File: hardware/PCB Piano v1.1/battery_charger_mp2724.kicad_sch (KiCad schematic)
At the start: 25 parts, among them J2 JST PH 4-PIN, J5 PinHeader 1x02 SMT, SW5 JST-PH 1x03 SMT, U15 MP2724GRH-0000-P

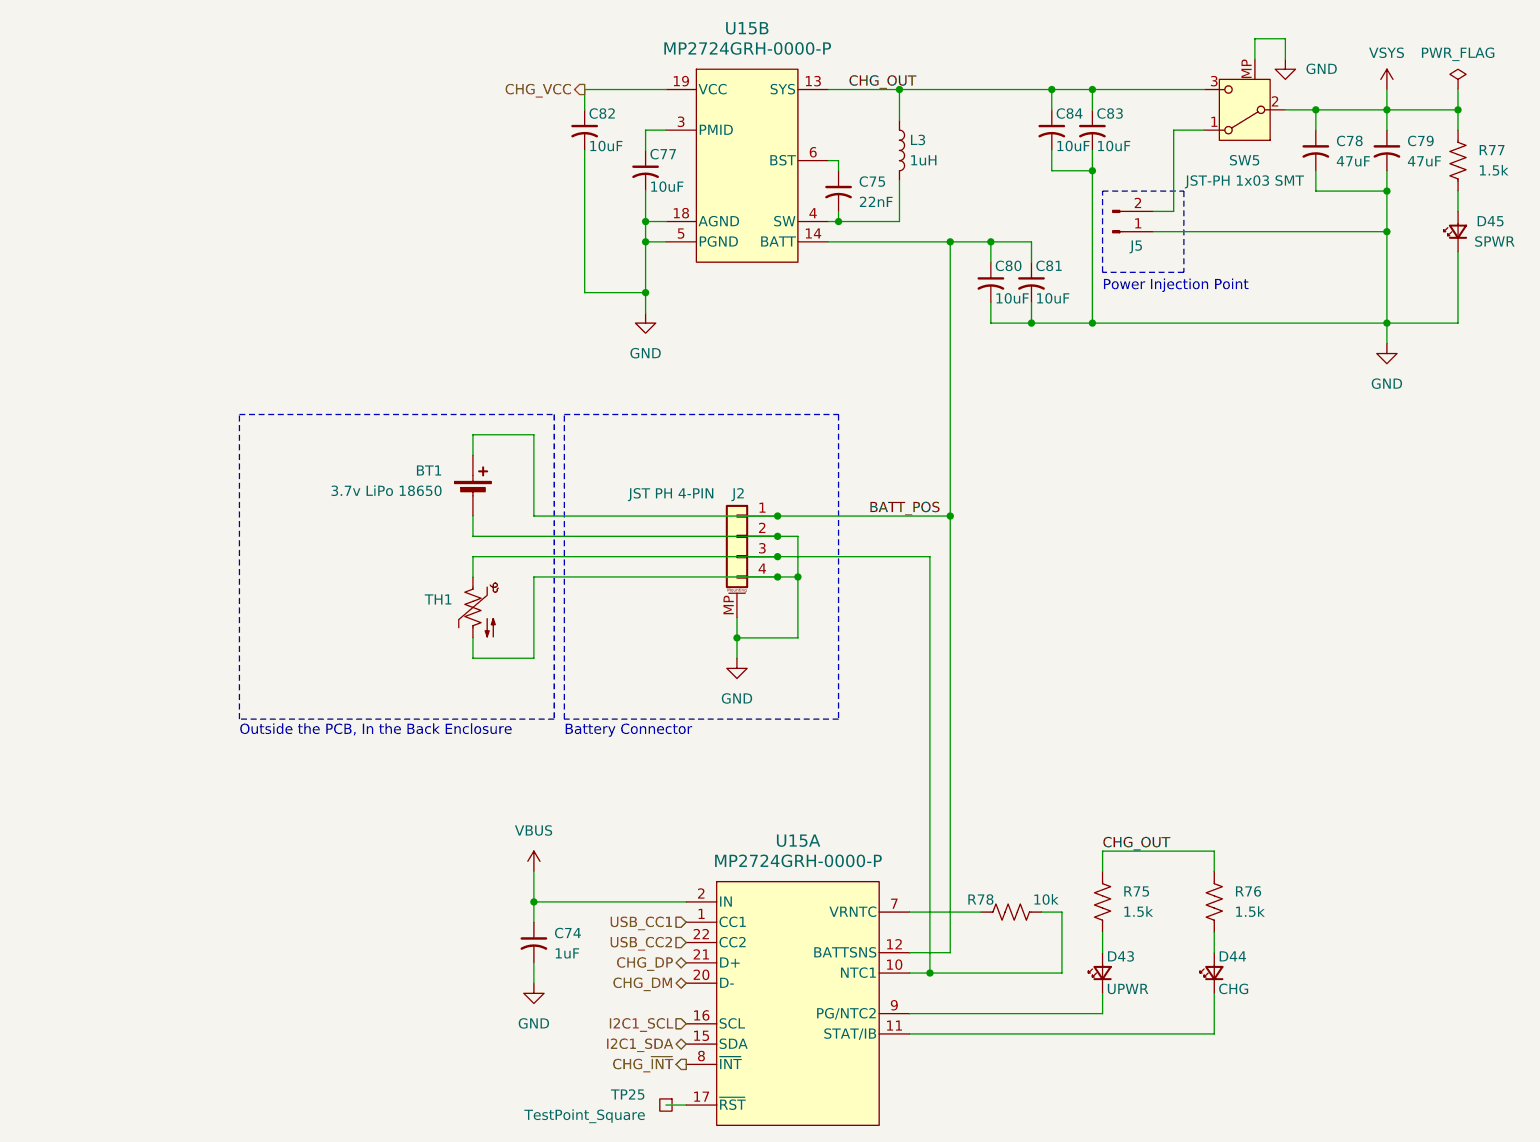
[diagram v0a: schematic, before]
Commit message: PCB Finalized and Ordered. Firmware near completion.
PCB Finalized and Ordered. Final revisions included fixing bugs on some peripheral chips. Also added an RTC circuit after realizing the SD card could benefit from adding file timestamps.

Firmware near completion. Still need to finalize some SD card operations. Synth audio core is finished and all the board peripheral chip drivers were completed.
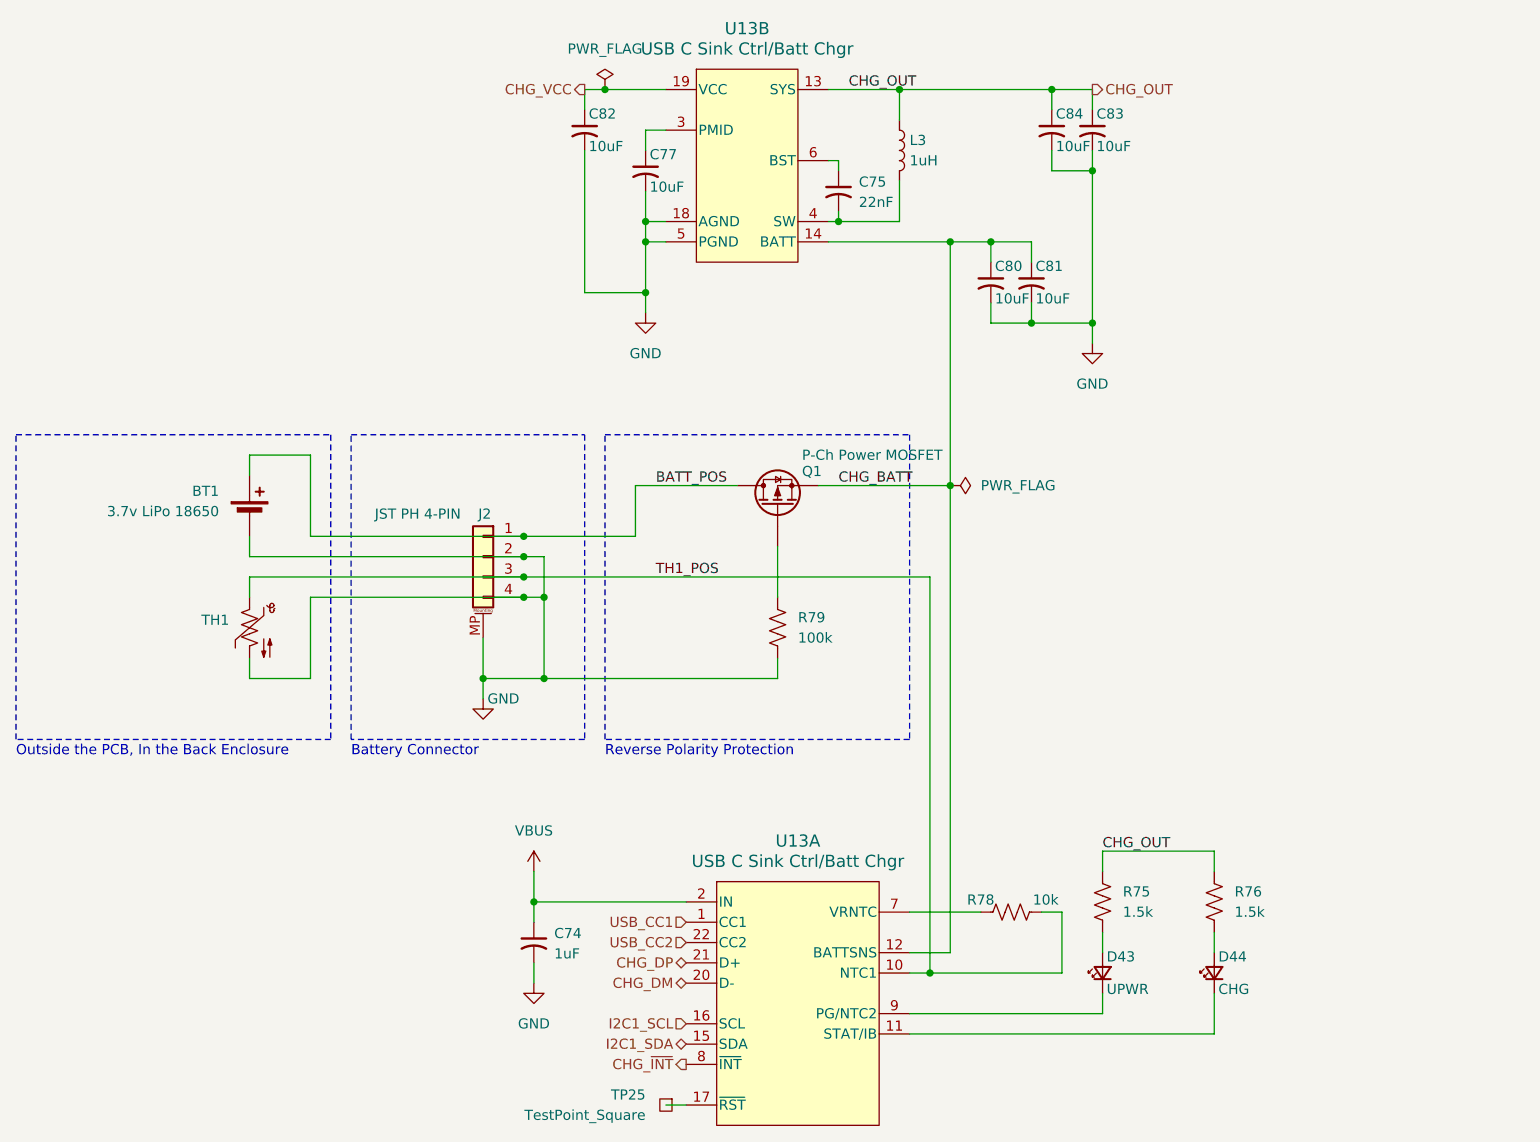
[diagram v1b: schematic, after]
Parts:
- removed C78, C79: 47uF, Capacitor_Tantalum_SMD:CP_EIA-3528-15_AVX-H, symbol Device:C_Small_US
- removed D45: LTST-C191TBKT, PCBPiano_Footprints:LED_0603_1608Metric, symbol Device:LED_Small
- removed J5: PinHeader 1x02 SMT, Connector_PinHeader_2.54mm:PinHeader_1x02_P2.54mm_Vertical_SMD_Pin1Left, symbol Connector:Conn_01x02_Pin
- removed R77: 1.5k, Resistor_SMD:R_0603_1608Metric, symbol Device:R_US
- removed SW5: JST-PH 1x03 SMT, Connector_JST:JST_PH_B3B-PH-SM4-TB_1x03-1MP_P2.00mm_Vertical, symbol PCB Piano Symbols:SW_SPDT_MP
- added Q1: P-Ch Power MOSFET, PCBPiano_Footprints:PPAK_3x3, symbol Device:Q_PMOS
- added R79: 100k, Resistor_SMD:R_0603_1608Metric, symbol Device:R_US
- C74: DigiKey_Part_Number (none) -> 1276-1184-1-ND; Manufacturer Part Number (none) -> CL10B105KA8NNNC; Volt Rating (none) -> 25V
- C75: footprint Capacitor_SMD:C_0603_1608Metric -> Capacitor_SMD:C_0805_2012Metric; DigiKey_Part_Number (none) -> 490-10516-1-ND; Manufacturer Part Number (none) -> GRM21B5C1H223JA01L; Volt Rating 16V -> 10V
- C77: DigiKey_Part_Number (none) -> 490-GRM21BZ71E106KE15LCT-ND; Manufacturer Part Number (none) -> GRM21BZ71E106KE15L
- C80, C81, C83, C84: DigiKey_Part_Number (none) -> 490-10516-1-ND; Manufacturer Part Number (none) -> GRM21BR71A106KA73L GRM21BR71A106KA73L GRM21BR71A106KA73L GR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; Volt Rating 16V -> 10V
- C82: DigiKey_Part_Number (none) -> 490-10516-1-ND; Manufacturer Part Number (none) -> GRM21BR71A106KA73L GRM21BR71A106KA73L GRM21BR71A106KA73L GR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
- D43, D44: value LTST-C191TBKT -> 3.3Vf, 104mcd; DigiKey_Part_Number (none) -> LTST-C191TBKT; Manufacturer Part Number (none) -> LTST-C191TBKT
- J2: Manufacturer Part Number (none) -> B4B-PH-SM4-TB
- TH1: value NXRT15XH103FA1B030 -> 10k Thermistor; DigiKey_Part_Number (none) -> NXRT15XH103FA1B030; Manufacturer Part Number (none) -> NXRT15XH103FA1B030
- U13: renamed from U15; value MP2724GRH-0000-P -> USB C Sink Ctrl/Batt Chgr; DigiKey_Part_Number (none) -> MP2724GRH-0000-P; Manufacturer Part Number (none) -> MP2724GRH-0000-P
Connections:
- net BATT_POS: now also Q1.D; no longer C80.1, C81.1, U13.12 (BATTSNS), U13.14 (BATT)
- net GND: now also R79.2
- net TH1_POS: now reaches J2.3 (Pin_3), R78.2, TH1.1, U13.10 (NTC1)
- new net: Q1.G, R79.1
- new net CHG_BATT: C80.1, C81.1, Q1.S, U13.12 (BATTSNS), U13.14 (BATT)
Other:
- note added: "Reverse Polarity Protection"
- note removed: "Power Injection Point"
- moved on the sheet: BT1, J2, TH1
